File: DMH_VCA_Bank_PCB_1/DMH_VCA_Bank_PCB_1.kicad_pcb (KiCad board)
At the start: 2 copper layers, 48 x 175 mm, 0 parts

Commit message: PCB 1 component placement in progress
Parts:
- added C1: 47uF, Capacitor_THT:CP_Radial_D5.0mm_P2.00mm, B.Cu at (56.8, 48.0)
- added C2: 47uF, Capacitor_THT:CP_Radial_D5.0mm_P2.00mm, B.Cu at (91.3, 48.0)
- added C3: 100nF, Capacitor_THT:C_Disc_D4.3mm_W1.9mm_P5.00mm, B.Cu at (77.5, 56.5)
- added C4: 100nF, Capacitor_THT:C_Disc_D4.3mm_W1.9mm_P5.00mm, B.Cu at (77.5, 78.8)
- added C5: 100nF, Capacitor_THT:C_Disc_D4.3mm_W1.9mm_P5.00mm, B.Cu at (77.5, 86.5)
- added C6: 100nF, Capacitor_THT:C_Disc_D4.3mm_W1.9mm_P5.00mm, B.Cu at (77.5, 108.8)
- added C7: 100nF, Capacitor_THT:C_Disc_D4.3mm_W1.9mm_P5.00mm, B.Cu at (77.5, 116.5)
- added C8: 100nF, Capacitor_THT:C_Disc_D4.3mm_W1.9mm_P5.00mm, B.Cu at (77.5, 138.8)
- added D1: SB140+, Diode_THT:D_DO-41_SOD81_P10.16mm_Horizontal, B.Cu at (62.5, 54.6)
- added D2: SB140-, Diode_THT:D_DO-41_SOD81_P10.16mm_Horizontal, B.Cu at (87.5, 44.4)
- added J1: TS_Jack_6.35mm_Sw, SynthStuff:CUI_MJ-63052A, F.Cu at (58.5, 159.2)
- added J10: TS_Jack_6.35mm_Sw, SynthStuff:CUI_MJ-63052A, F.Cu at (58.5, 208.8)
- added J100: IDC_02x05, SynthStuff:IDC-Header_2x05_P2.54mm_Vertical_Eurorack, B.Cu at (80.1, 48.8)
- added J11: TS_Jack_6.35mm_Sw, SynthStuff:CUI_MJ-63052A, F.Cu at (75.0, 208.8)
- added J12: TS_Jack_6.35mm_Sw, SynthStuff:CUI_MJ-63052A, F.Cu at (91.5, 208.8)
- added J2: TS_Jack_6.35mm_Sw, SynthStuff:CUI_MJ-63052A, F.Cu at (75.0, 159.2)
- added J200: IDC_02x08, SynthStuff:IDC-Header_2x08_P2.54mm_Vertical_BackBone, B.Cu at (56.9, 145.7)
- added J3: TS_Jack_6.35mm_Sw, SynthStuff:CUI_MJ-63052A, F.Cu at (91.5, 159.2)
- added J4: TS_Jack_6.35mm_Sw, SynthStuff:CUI_MJ-63052A, F.Cu at (58.5, 175.8)
- added J5: TS_Jack_6.35mm_Sw, SynthStuff:CUI_MJ-63052A, F.Cu at (75.0, 175.8)
- added J50: Conn_01x06, Connector_PinHeader_2.54mm:PinHeader_1x06_P2.54mm_Vertical, F.Cu at (53.0, 48.0)
- added J6: TS_Jack_6.35mm_Sw, SynthStuff:CUI_MJ-63052A, F.Cu at (91.5, 175.8)
- added J60: Conn_01x06, Connector_PinHeader_2.54mm:PinHeader_1x06_P2.54mm_Vertical, F.Cu at (97.0, 77.0)
- added J7: TS_Jack_6.35mm_Sw, SynthStuff:CUI_MJ-63052A, F.Cu at (58.5, 192.2)
- added J70: Conn_01x06, Connector_PinHeader_2.54mm:PinHeader_1x06_P2.54mm_Vertical, F.Cu at (53.0, 103.0)
- added J8: TS_Jack_6.35mm_Sw, SynthStuff:CUI_MJ-63052A, F.Cu at (75.0, 192.2)
- added J80: Conn_01x06, Connector_PinHeader_2.54mm:PinHeader_1x06_P2.54mm_Vertical, F.Cu at (97.0, 132.0)
- added J9: TS_Jack_6.35mm_Sw, SynthStuff:CUI_MJ-63052A, F.Cu at (91.5, 192.2)
- added Q1: BC548, Package_TO_SOT_THT:TO-92L_Inline_Wide, B.Cu at (54.2, 63.7)
- added Q2: BC548, Package_TO_SOT_THT:TO-92L_Inline_Wide, B.Cu at (54.2, 71.0)
- added Q3: BC548, Package_TO_SOT_THT:TO-92L_Inline_Wide, B.Cu at (95.8, 64.0)
- added Q4: BC548, Package_TO_SOT_THT:TO-92L_Inline_Wide, B.Cu at (95.8, 71.3)
- added Q5: BC548, Package_TO_SOT_THT:TO-92L_Inline_Wide, B.Cu at (54.5, 128.4)
- added Q6: BC548, Package_TO_SOT_THT:TO-92L_Inline_Wide, B.Cu at (54.5, 135.7)
- added Q7: BC548, Package_TO_SOT_THT:TO-92L_Inline_Wide, B.Cu at (95.8, 120.8)
- added Q8: BC548, Package_TO_SOT_THT:TO-92L_Inline_Wide, B.Cu at (95.8, 128.1)
- added R1: 20k, Resistor_THT:R_Axial_DIN0207_L6.3mm_D2.5mm_P2.54mm_Vertical, B.Cu at (57.2, 56.3)
- added R10: 100R, Resistor_THT:R_Axial_DIN0207_L6.3mm_D2.5mm_P2.54mm_Vertical, F.Cu at (30.8, 81.5)
- added R11: 100R, Resistor_THT:R_Axial_DIN0207_L6.3mm_D2.5mm_P2.54mm_Vertical, F.Cu at (30.8, 85.6)
- added R12: 10k, Resistor_THT:R_Axial_DIN0207_L6.3mm_D2.5mm_P2.54mm_Vertical, F.Cu at (30.8, 89.7)
- added R13: 33k, Resistor_THT:R_Axial_DIN0207_L6.3mm_D2.5mm_P2.54mm_Vertical, F.Cu at (107.4, 70.4)
- added R14: 100k, Resistor_THT:R_Axial_DIN0207_L6.3mm_D2.5mm_P2.54mm_Vertical, F.Cu at (36.9, 77.5)
- added R15: 100k, Resistor_THT:R_Axial_DIN0207_L6.3mm_D2.5mm_P2.54mm_Vertical, F.Cu at (36.9, 81.5)
- added R16: 20k, Resistor_THT:R_Axial_DIN0207_L6.3mm_D2.5mm_P2.54mm_Vertical, F.Cu at (107.4, 74.5)
- added R17: 20k, Resistor_THT:R_Axial_DIN0207_L6.3mm_D2.5mm_P2.54mm_Vertical, F.Cu at (107.4, 78.5)
- added R18: 100k, Resistor_THT:R_Axial_DIN0207_L6.3mm_D2.5mm_P2.54mm_Vertical, F.Cu at (107.4, 82.5)
- added R19: 10k, Resistor_THT:R_Axial_DIN0207_L6.3mm_D2.5mm_P2.54mm_Vertical, F.Cu at (113.6, 70.4)
- added R2: 20k, Resistor_THT:R_Axial_DIN0207_L6.3mm_D2.5mm_P2.54mm_Vertical, F.Cu at (18.5, 81.5)
- added R20: 1k, Resistor_THT:R_Axial_DIN0207_L6.3mm_D2.5mm_P2.54mm_Vertical, F.Cu at (113.6, 74.5)
- added R21: 10k, Resistor_THT:R_Axial_DIN0207_L6.3mm_D2.5mm_P2.54mm_Vertical, F.Cu at (113.6, 78.5)
- added R22: 100k, Resistor_THT:R_Axial_DIN0207_L6.3mm_D2.5mm_P2.54mm_Vertical, F.Cu at (113.6, 82.5)
- added R23: 100k, Resistor_THT:R_Axial_DIN0207_L6.3mm_D2.5mm_P2.54mm_Vertical, F.Cu at (119.7, 70.4)
- added R24: 100k, Resistor_THT:R_Axial_DIN0207_L6.3mm_D2.5mm_P2.54mm_Vertical, F.Cu at (119.7, 74.5)
- added R25: 100R, Resistor_THT:R_Axial_DIN0207_L6.3mm_D2.5mm_P2.54mm_Vertical, F.Cu at (119.7, 78.5)
- added R26: 100R, Resistor_THT:R_Axial_DIN0207_L6.3mm_D2.5mm_P2.54mm_Vertical, F.Cu at (119.7, 82.5)
- added R27: 10k, Resistor_THT:R_Axial_DIN0207_L6.3mm_D2.5mm_P2.54mm_Vertical, F.Cu at (125.8, 70.4)
- added R28: 33k, Resistor_THT:R_Axial_DIN0207_L6.3mm_D2.5mm_P2.54mm_Vertical, F.Cu at (13.2, 124.9)
- added R29: 100k, Resistor_THT:R_Axial_DIN0207_L6.3mm_D2.5mm_P2.54mm_Vertical, F.Cu at (125.8, 74.5)
- added R3: 100k, Resistor_THT:R_Axial_DIN0207_L6.3mm_D2.5mm_P2.54mm_Vertical, F.Cu at (18.5, 85.6)
- added R30: 100k, Resistor_THT:R_Axial_DIN0207_L6.3mm_D2.5mm_P2.54mm_Vertical, F.Cu at (125.8, 78.5)
- added R31: 100k, Resistor_THT:R_Axial_DIN0207_L6.3mm_D2.5mm_P2.54mm_Vertical, F.Cu at (13.2, 128.9)
- added R32: 100k, Resistor_THT:R_Axial_DIN0207_L6.3mm_D2.5mm_P2.54mm_Vertical, F.Cu at (13.2, 133.0)
- added R33: 100k, Resistor_THT:R_Axial_DIN0207_L6.3mm_D2.5mm_P2.54mm_Vertical, F.Cu at (13.2, 137.1)
- added R34: 100R, Resistor_THT:R_Axial_DIN0207_L6.3mm_D2.5mm_P2.54mm_Vertical, F.Cu at (19.4, 124.9)
- added R35: 20k, Resistor_THT:R_Axial_DIN0207_L6.3mm_D2.5mm_P2.54mm_Vertical, F.Cu at (19.4, 128.9)
- added R36: 10k, Resistor_THT:R_Axial_DIN0207_L6.3mm_D2.5mm_P2.54mm_Vertical, F.Cu at (19.4, 133.0)
- added R37: 20k, Resistor_THT:R_Axial_DIN0207_L6.3mm_D2.5mm_P2.54mm_Vertical, F.Cu at (19.4, 137.1)
- added R38: 100R, Resistor_THT:R_Axial_DIN0207_L6.3mm_D2.5mm_P2.54mm_Vertical, F.Cu at (25.5, 124.9)
- added R39: 10k, Resistor_THT:R_Axial_DIN0207_L6.3mm_D2.5mm_P2.54mm_Vertical, F.Cu at (25.5, 128.9)
- added R4: 10k, Resistor_THT:R_Axial_DIN0207_L6.3mm_D2.5mm_P2.54mm_Vertical, F.Cu at (18.5, 89.7)
- added R40: 10k, Resistor_THT:R_Axial_DIN0207_L6.3mm_D2.5mm_P2.54mm_Vertical, F.Cu at (25.5, 133.0)
- added R41: 100k, Resistor_THT:R_Axial_DIN0207_L6.3mm_D2.5mm_P2.54mm_Vertical, F.Cu at (25.5, 137.1)
- added R42: 100k, Resistor_THT:R_Axial_DIN0207_L6.3mm_D2.5mm_P2.54mm_Vertical, F.Cu at (31.6, 124.9)
- added R43: 33k, Resistor_THT:R_Axial_DIN0207_L6.3mm_D2.5mm_P2.54mm_Vertical, F.Cu at (110.0, 123.7)
- added R44: 100k, Resistor_THT:R_Axial_DIN0207_L6.3mm_D2.5mm_P2.54mm_Vertical, F.Cu at (31.6, 128.9)
- added R45: 1k, Resistor_THT:R_Axial_DIN0207_L6.3mm_D2.5mm_P2.54mm_Vertical, F.Cu at (31.6, 133.0)
- added R46: 100k, Resistor_THT:R_Axial_DIN0207_L6.3mm_D2.5mm_P2.54mm_Vertical, F.Cu at (110.0, 127.7)
- added R47: 100k, Resistor_THT:R_Axial_DIN0207_L6.3mm_D2.5mm_P2.54mm_Vertical, F.Cu at (110.0, 131.8)
- added R48: 100k, Resistor_THT:R_Axial_DIN0207_L6.3mm_D2.5mm_P2.54mm_Vertical, F.Cu at (110.0, 135.8)
- added R49: 100R, Resistor_THT:R_Axial_DIN0207_L6.3mm_D2.5mm_P2.54mm_Vertical, F.Cu at (116.1, 123.7)
- added R5: 1k, Resistor_THT:R_Axial_DIN0207_L6.3mm_D2.5mm_P2.54mm_Vertical, F.Cu at (24.6, 77.5)
- added R50: 20k, Resistor_THT:R_Axial_DIN0207_L6.3mm_D2.5mm_P2.54mm_Vertical, F.Cu at (116.1, 127.7)
- added R51: 10k, Resistor_THT:R_Axial_DIN0207_L6.3mm_D2.5mm_P2.54mm_Vertical, F.Cu at (116.1, 131.8)
- added R52: 20k, Resistor_THT:R_Axial_DIN0207_L6.3mm_D2.5mm_P2.54mm_Vertical, F.Cu at (116.1, 135.8)
- added R57: 100R, Resistor_THT:R_Axial_DIN0207_L6.3mm_D2.5mm_P2.54mm_Vertical, F.Cu at (122.2, 123.7)
- added R58: 10k, Resistor_THT:R_Axial_DIN0207_L6.3mm_D2.5mm_P2.54mm_Vertical, F.Cu at (122.2, 127.7)
- added R59: 10k, Resistor_THT:R_Axial_DIN0207_L6.3mm_D2.5mm_P2.54mm_Vertical, F.Cu at (122.2, 131.8)
- added R6: 10k, Resistor_THT:R_Axial_DIN0207_L6.3mm_D2.5mm_P2.54mm_Vertical, F.Cu at (24.6, 81.5)
- added R60: 100k, Resistor_THT:R_Axial_DIN0207_L6.3mm_D2.5mm_P2.54mm_Vertical, F.Cu at (122.2, 135.8)
- added R61: 100k, Resistor_THT:R_Axial_DIN0207_L6.3mm_D2.5mm_P2.54mm_Vertical, F.Cu at (128.4, 123.7)
- added R62: 33k, Resistor_THT:R_Axial_DIN0207_L6.3mm_D2.5mm_P2.54mm_Vertical, F.Cu at (36.9, 85.6)
- added R63: 100k, Resistor_THT:R_Axial_DIN0207_L6.3mm_D2.5mm_P2.54mm_Vertical, F.Cu at (36.9, 89.7)
- added R64: 100k, Resistor_THT:R_Axial_DIN0207_L6.3mm_D2.5mm_P2.54mm_Vertical, F.Cu at (125.8, 82.5)
- added R65: 100k, Resistor_THT:R_Axial_DIN0207_L6.3mm_D2.5mm_P2.54mm_Vertical, F.Cu at (31.6, 137.1)
- added R66: 100k, Resistor_THT:R_Axial_DIN0207_L6.3mm_D2.5mm_P2.54mm_Vertical, F.Cu at (128.4, 127.7)
- added R67: 100k, Resistor_THT:R_Axial_DIN0207_L6.3mm_D2.5mm_P2.54mm_Vertical, F.Cu at (128.4, 131.8)
- added R68: 1k, Resistor_THT:R_Axial_DIN0207_L6.3mm_D2.5mm_P2.54mm_Vertical, F.Cu at (128.4, 135.8)
- added R7: 100k, Resistor_THT:R_Axial_DIN0207_L6.3mm_D2.5mm_P2.54mm_Vertical, F.Cu at (24.6, 85.6)
- added R8: 100k, Resistor_THT:R_Axial_DIN0207_L6.3mm_D2.5mm_P2.54mm_Vertical, F.Cu at (24.6, 89.7)
- added R9: 100k, Resistor_THT:R_Axial_DIN0207_L6.3mm_D2.5mm_P2.54mm_Vertical, F.Cu at (30.8, 77.5)
- added RV1: 100k, Potentiometer_THT:Potentiometer_Bourns_3296W_Vertical, B.Cu at (64.5, 60.8)
- added RV10: 50k, Potentiometer_THT:Potentiometer_Bourns_3296W_Vertical, B.Cu at (64.5, 82.5)
- added RV11: 50k, Potentiometer_THT:Potentiometer_Bourns_3296W_Vertical, B.Cu at (90.5, 82.5)
- added RV12: 50k, Potentiometer_THT:Potentiometer_Bourns_3296W_Vertical, B.Cu at (90.5, 112.5)
- added RV15: 50k, Potentiometer_THT:Potentiometer_Bourns_3296W_Vertical, B.Cu at (64.5, 112.5)
- added RV16: 100k, Potentiometer_THT:Potentiometer_Bourns_3296W_Vertical, B.Cu at (90.5, 138.8)
- added RV2: 100k, Potentiometer_THT:Potentiometer_Bourns_3296W_Vertical, B.Cu at (90.5, 60.8)
- added RV3: 100k, Potentiometer_THT:Potentiometer_Bourns_3296W_Vertical, B.Cu at (64.5, 138.8)
- added U1: TL074, Package_DIP:DIP-14_W7.62mm_Socket, B.Cu at (78.8, 60.0)
- added U2: TL074, Package_DIP:DIP-14_W7.62mm_Socket, B.Cu at (78.8, 90.0)
- added U3: TL074, Package_DIP:DIP-14_W7.62mm_Socket, B.Cu at (78.8, 120.0)
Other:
- board text added: "Mk1.0 - Month 2025"
- board text removed: "Mk2.0 - Month 2025"

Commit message: PCB 1 component placement in progress
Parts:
- R10, R11, R12, R13, R14, R15, R16, R17, R18, R19, R2, R20, R21, R22, R23, R24, R25, R26, R27, R28, R29, R3, R30, R31, R32, R33, R34, R35, R36, R37, R38, R39, R4, R40, R41, R42, R43, R44, R45, R46, R47, R48, R49, R5, R50, R51, R52, R57, R58, R59, R6, R60, R61, R62, R63, R64, R65, R66, R67, R68, R7, R8, R9: moved to B.Cu
- moved R3 69.1 mm to (80.5, 55.2)
- moved R5 60.1 mm to (82.0, 59.7), turned to -90 degrees
- moved R29 51.7 mm to (82.5, 102.7), turned to -90 degrees
- moved R4 48.3 mm to (61.2, 67.3), turned to 90 degrees
- moved R18 47.4 mm to (69.5, 54.0), turned to 180 degrees
- moved R7 46.9 mm to (67.8, 67.3), turned to 90 degrees
- moved R27 46.2 mm to (81.0, 81.5), turned to -90 degrees
- moved R6 42.4 mm to (64.5, 67.3), turned to 90 degrees
- moved R2 42.0 mm to (58.0, 67.3), turned to 90 degrees
- moved R64 41.4 mm to (84.7, 87.0)
- moved R62 40.5 mm to (68.0, 59.7), turned to -90 degrees
- moved R26 39.6 mm to (91.7, 54.5)
- moved R12 39.1 mm to (69.0, 81.5), turned to -90 degrees
- moved R11 38.9 mm to (67.8, 73.5), turned to -90 degrees
- moved R8 37.1 mm to (58.0, 73.5), turned to -90 degrees
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
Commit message: Update DMH_VCA_Bank_PCB_1.kicad_pcb
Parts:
- moved R33 23.5 mm to (29.7, 104.2)
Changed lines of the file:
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@@
 	(footprint "Resistor_THT:R_Axial_DIN0207_L6.3mm_D2.5mm_P2.54mm_Vertical"
 		(layer "B.Cu")
-		(at 18.455 124.9)
+		(at 29.705 104.25)
 		(descr "Resistor, Axial_DIN0207 series, Axial, Vertical, pin pitch=2.54mm, 0.25W = 1/4W, length*diameter=6.3*2.5mm^2, http://cdn-reichelt.de/documents/datenblatt/B400/1_4W%23YAG.pdf")
 		(tags "Resistor Axial_DIN0207 series Axial Vertical pin pitch 2.54mm 0.25W = 1/4W length 6.3mm diameter 2.5mm")

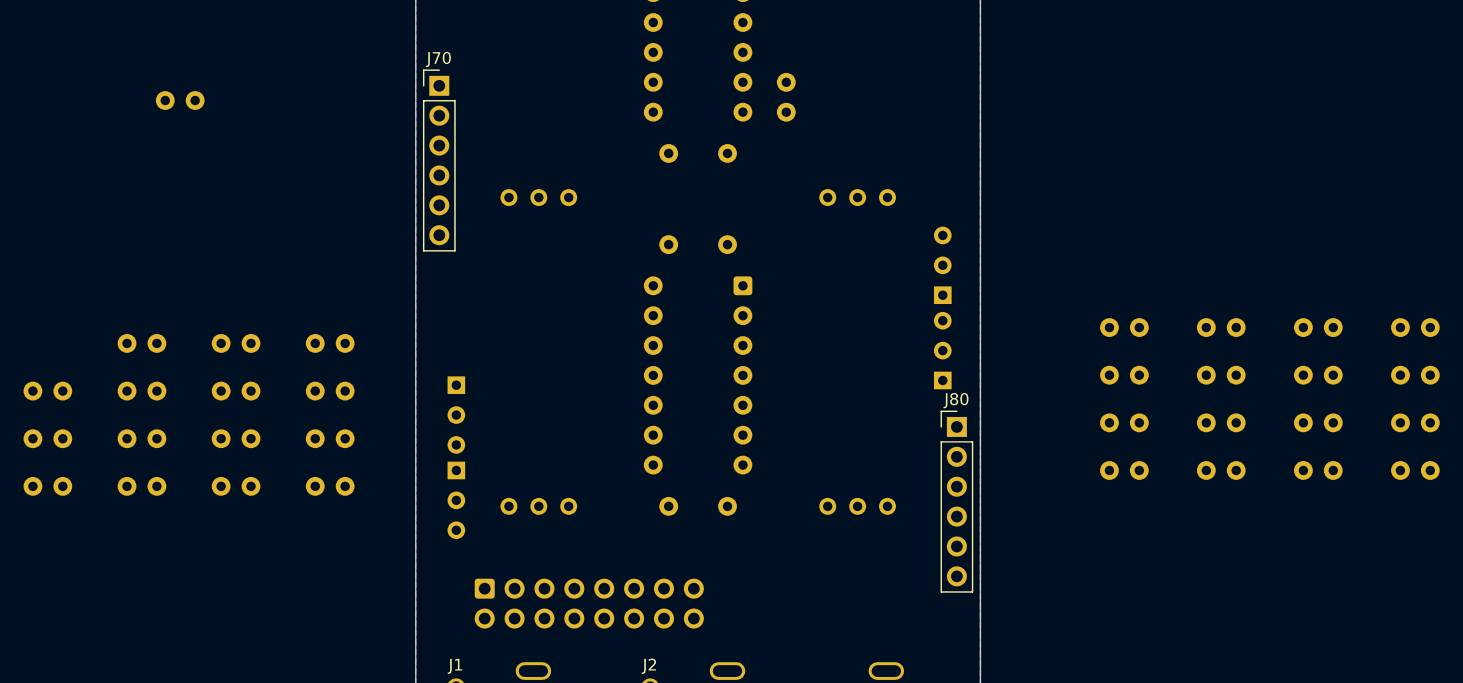
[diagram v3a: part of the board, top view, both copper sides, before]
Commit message: PCB 1 component placement done
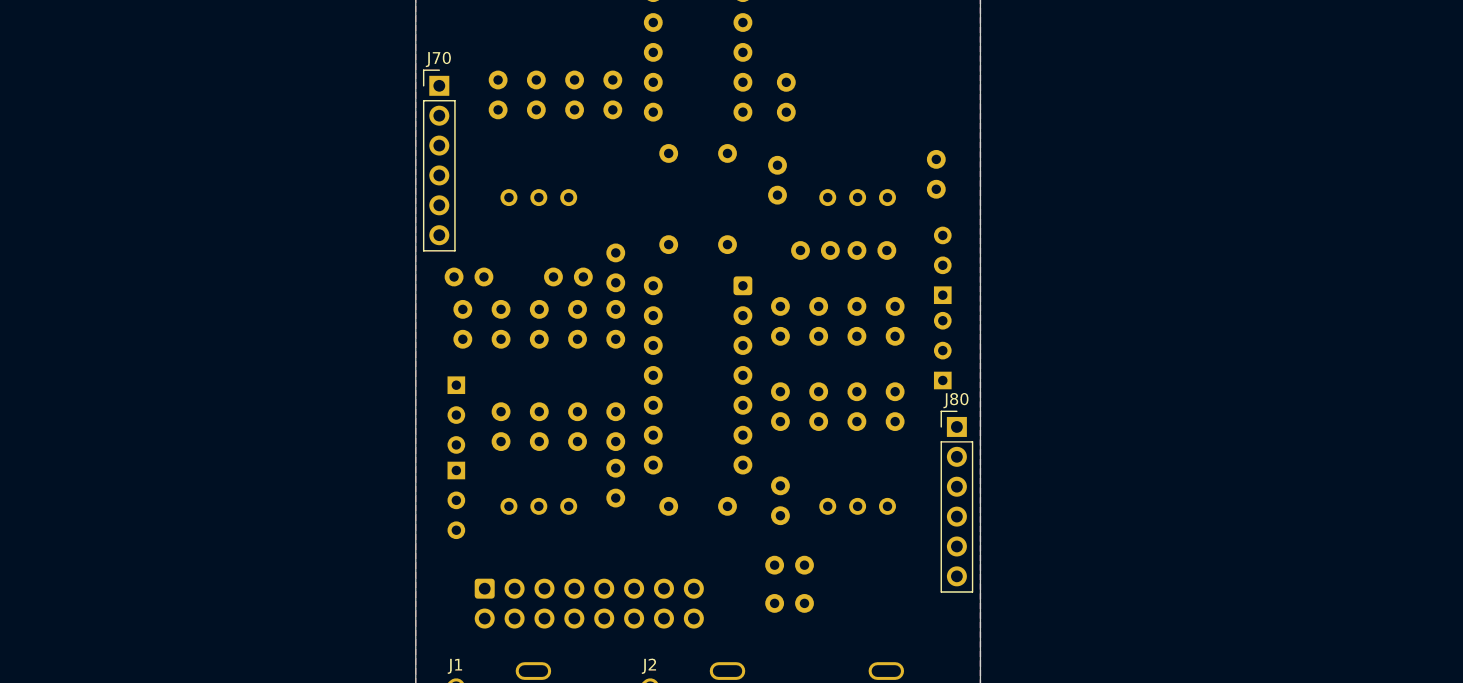
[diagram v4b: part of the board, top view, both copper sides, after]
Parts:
- moved R66 67.0 mm to (68.0, 138.0), turned to 90 degrees
- moved R32 65.4 mm to (81.8, 112.3), turned to 90 degrees
- moved R68 55.8 mm to (84.0, 147.0), turned to 180 degrees
- moved R28 53.4 mm to (61.2, 105.0), turned to 90 degrees
- moved R67 52.8 mm to (82.0, 124.3), turned to 90 degrees
- moved R31 48.4 mm to (58.0, 105.0), turned to 90 degrees
- moved R47 47.9 mm to (67.8, 105.0), turned to 90 degrees
- moved R60 47.2 mm to (82.0, 139.5), turned to 90 degrees
- moved R61 46.1 mm to (95.2, 111.8), turned to 90 degrees
- moved R58 45.2 mm to (83.7, 117.0)
- moved R57 43.2 mm to (84.0, 143.8), turned to 180 degrees
- moved R59 41.3 mm to (85.2, 124.3), turned to 90 degrees
- moved R33 38.9 mm to (58.2, 130.7), turned to -90 degrees
- moved R34 35.6 mm to (61.5, 130.7), turned to -90 degrees
- moved R36 35.3 mm to (61.5, 124.5), turned to 90 degrees
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
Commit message: Routing in progress
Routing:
- net +12V: track 0.00 -> 266.3 mm
- net -12V: track 0.00 -> 172.2 mm
- net /Inputs and Outputs/CV Amt A Pot: track 0.00 -> 78.9 mm
- net Net-(Q3-E): track 0.00 -> 42.1 mm
- net Net-(U1D--): track 0.00 -> 31.2 mm
- net Net-(U1A--): track 0.00 -> 28.6 mm
- net Net-(R18-Pad1): track 0.00 -> 28.2 mm
- net Net-(U1D-+): track 0.00 -> 27.4 mm
- net Net-(Q4-B): track 0.00 -> 27.4 mm
- net /Inputs and Outputs/CV Amt B Pot: track 0.00 -> 24.8 mm
- net Net-(Q4-C): track 0.00 -> 24.2 mm
- net Net-(U2A--): track 0.00 -> 18.2 mm
- net Net-(Q3-B): track 0.00 -> 17.3 mm
- net Net-(Q1-C): track 0.00 -> 17.1 mm
- net /Inputs and Outputs/CV A Jack: track 0.00 -> 16.7 mm
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
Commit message: Routing in progress
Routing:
- net Net-(U3D--): track 0.00 -> 55.4 mm
- net Net-(R65-Pad1): track 0.00 -> 55.3 mm
- net Net-(U2D--): track 0.00 -> 46.2 mm
- net Net-(R47-Pad2): track 0.00 -> 45.3 mm
- net Net-(U3A--): track 0.00 -> 44.9 mm
- net Net-(Q8-B): track 0.00 -> 42.8 mm
- net Net-(U3B-+): track 0.00 -> 40.8 mm
- net Net-(U2C--): track 0.00 -> 33.9 mm
- net Net-(R66-Pad1): track 0.00 -> 33.7 mm
- net Net-(R32-Pad2): track 0.00 -> 33.3 mm
- net Net-(U2C-+): track 0.00 -> 33.2 mm
- net /Inputs and Outputs/CV Amt D Pot: track 0.00 -> 32.0 mm
- net Net-(Q1-E): track 0.00 -> 31.5 mm
- net Net-(U1C--): track 0.00 -> 30.3 mm
- net Net-(R27-Pad1): track 0.00 -> 29.2 mm
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
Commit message: Routing in progress
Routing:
- net Net-(J200-Pin_11): track 0.00 -> 51.0 mm
- net Net-(J200-Pin_9): track 0.00 -> 39.2 mm
- net Net-(J200-Pin_3): track 0.00 -> 35.4 mm
- net Net-(J200-Pin_2): track 0.00 -> 26.9 mm
- net Net-(J200-Pin_1): track 0.00 -> 8.72 mm
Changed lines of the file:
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@@
+	)
+	(segment
+		(start 58.249 149.999)
+		(end 61 152.75)
+		(width 0.2)
+		(layer "F.Cu")
+		(net 6)
+	)
+	(segment
+		(start 58.249 147.1365)
+		(end 58.249 149.999)
+		(width 0.2)
+		(layer "F.Cu")
+		(net 6)
+	)
+	(segment
+		(start 56.86 145.7475)
+		(end 58.249 147.1365)
+		(width 0.2)
+		(layer "F.Cu")
+		(net 6)
+	)
+	(segment
+		(start 77.5 145.4)
+		(end 77.5 152.75)
+		(width 0.2)
+		(layer "F.Cu")
+		(net 8)
+	)
+	(segment
+		(start 75.9 143.8)
+		(end 77.5 145.4)
+		(width 0.2)
+		(layer "F.Cu")
+		(net 8)
+	)
+	(segment
+		(start 61.3475 143.8)
+		(end 75.9 143.8)
+		(width 0.2)
+		(layer "F.Cu")
+		(net 8)
+	)
+	(segment
+		(start 59.4 145.7475)
+		(end 61.3475 143.8)
+		(width 0.2)
+		(layer "F.Cu")
+		(net 8)
 	)
 	(segment
@@
 	)
 	(segment
+		(start 75.6 152.2)
+		(end 75.6 153.095995)
+		(width 0.2)
+		(layer "F.Cu")
+		(net 11)
+	)
+	(segment
+		(start 63.4865 144.201)
+		(end 75.7339 144.201)
+		(width 0.2)
+		(layer "F.Cu")
+		(net 11)
+	)
+	(segment
+		(start 79.254005 156.75)
+		(end 85 156.75)
+		(width 0.2)
+		(layer "F.Cu")
+		(net 11)
+	)
+	(segment
+		(start 75.7339 144.201)
+		(end 77.099 145.5661)
+		(width 0.2)
+		(layer "F.Cu")
+		(net 11)
+	)
+	(segment
+		(start 77.099 150.701)
+		(end 75.6 152.2)
+		(width 0.2)
+		(layer "F.Cu")
+		(net 11)
+	)
+	(segment
+		(start 77.099 145.5661)
+		(end 77.099 150.701)
+		(width 0.2)
+		(layer "F.Cu")
+		(net 11)
+	)
+	(segment
+		(start 61.94 145.7475)
+		(end 63.4865 144.201)
+		(width 0.2)
+		(layer "F.Cu")
+		(net 11)
+	)
+	(segment
+		(start 75.6 153.095995)
+		(end 79.254005 156.75)
+		(width 0.2)
+		(layer "F.Cu")
+		(net 11)
+	)
+	(segment
 		(start 94.425 84.62)
 		(end 97 84.62)
@@
 		(layer "F.Cu")
 		(net 15)
+	)
+	(segment
+		(start 56.86 181.61)
+		(end 61 185.75)
+		(width 0.2)
+		(layer "B.Cu")
+		(net 18)
+	)
+	(segment
+		(start 56.86 148.2875)
+		(end 56.86 181.61)
+		(width 0.2)
+		(layer "B.Cu")
+		(net 18)
 	)
 	(segment
@@
 	)
 	(segment
+		(start 61.94 148.2875)
+		(end 61.94 150.64)
+		(width 0.2)
+		(layer "F.Cu")
+		(net 22)
+	)
+	(segment
+		(start 74.6 163.3)
+		(end 74.6 179.35)
+		(width 0.2)
+		(layer "F.Cu")
+		(net 22)
+	)
+	(segment
+		(start 74.6 179.35)
+		(end 85 189.75)
+		(width 0.2)
+		(layer "F.Cu")
+		(net 22)
+	)
+	(segment
+		(start 61.94 150.64)
+		(end 74.6 163.3)
+		(width 0.2)
+		(layer "F.Cu")
+		(net 22)
+	)
+	(segment

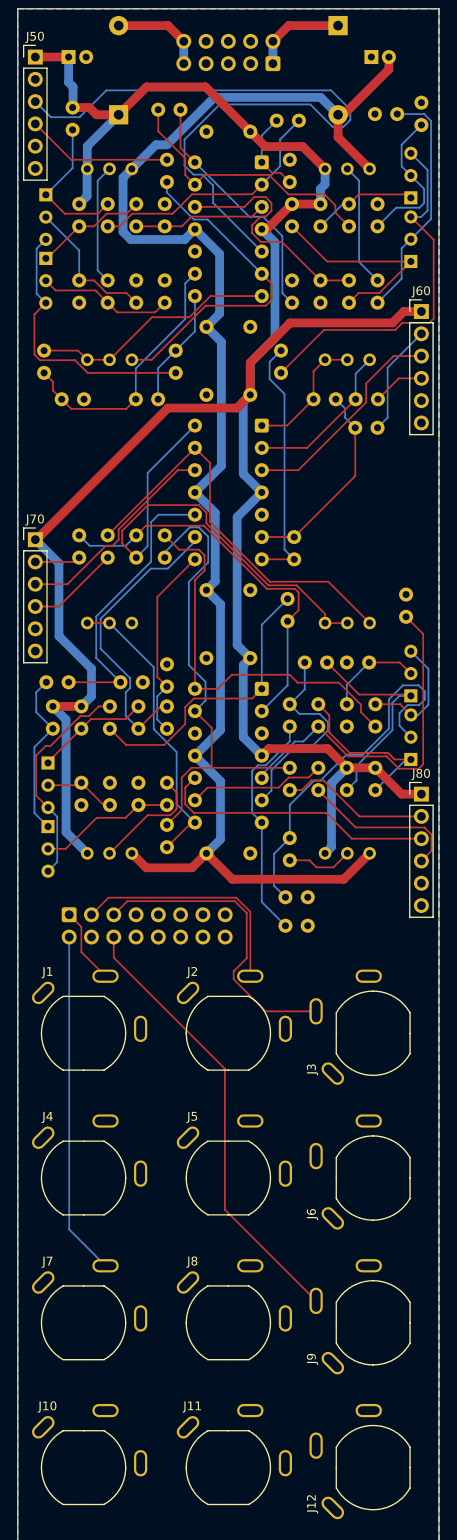
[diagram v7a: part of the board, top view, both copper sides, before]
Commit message: Routing done but needs error correction
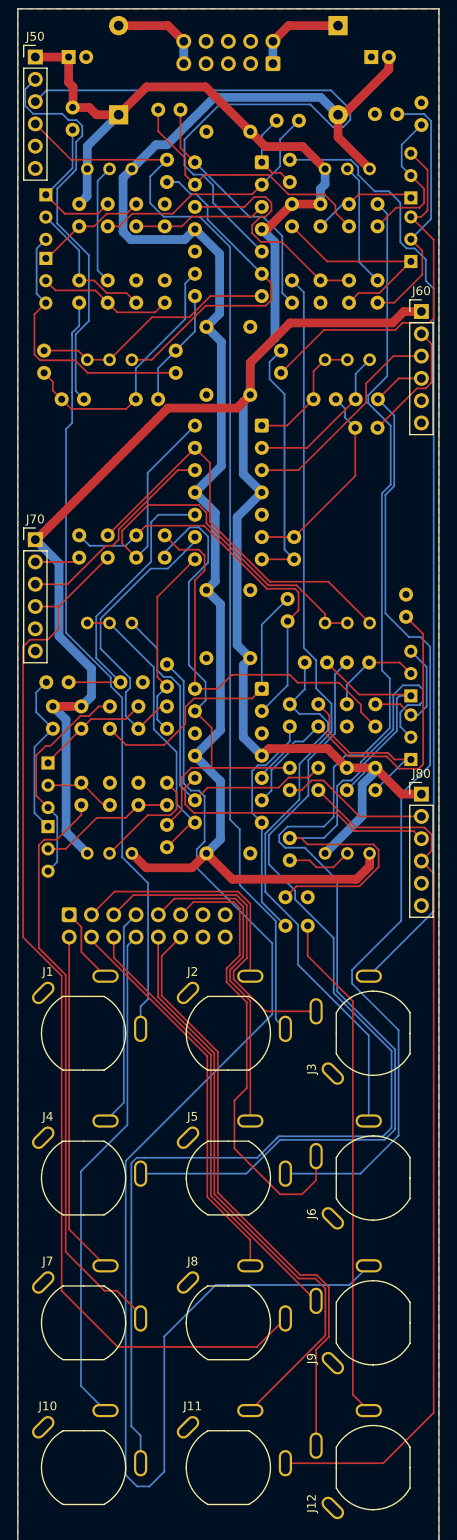
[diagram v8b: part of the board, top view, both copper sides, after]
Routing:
- net /Inputs and Outputs/Input B Jack: track 0.00 -> 155.3 mm
- net /Inputs and Outputs/Output C Jack: track 0.00 -> 153.2 mm
- net /Inputs and Outputs/Input D Jack: track 0.00 -> 128.5 mm
- net /Inputs and Outputs/CV C Jack: track 10.6 -> 122.7 mm
- net /Inputs and Outputs/CV A Jack: track 16.7 -> 125.3 mm
- net /Inputs and Outputs/CV B Jack: track 5.94 -> 114.5 mm
- net /Inputs and Outputs/Output A Jack: track 0.00 -> 108.5 mm
- net /Inputs and Outputs/Output B Jack: track 0.00 -> 105.7 mm
- net /Inputs and Outputs/Input A Jack: track 0.00 -> 87.6 mm
- net /Inputs and Outputs/CV D Jack: track 18.5 -> 101.2 mm
- net Net-(J200-Pin_14): track 0.00 -> 68.5 mm
- net /Inputs and Outputs/Input C Jack: track 0.00 -> 67.0 mm
- net Net-(J200-Pin_13): track 0.00 -> 66.5 mm
- net /Inputs and Outputs/Output D Jack: track 0.00 -> 58.1 mm
- net Net-(J200-Pin_12): track 0.00 -> 57.7 mm
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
